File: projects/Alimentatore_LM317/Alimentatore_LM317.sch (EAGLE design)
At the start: 19 parts, among them X1 SMKDSP_1,5/3, X2 SMKDSP_1,5/3

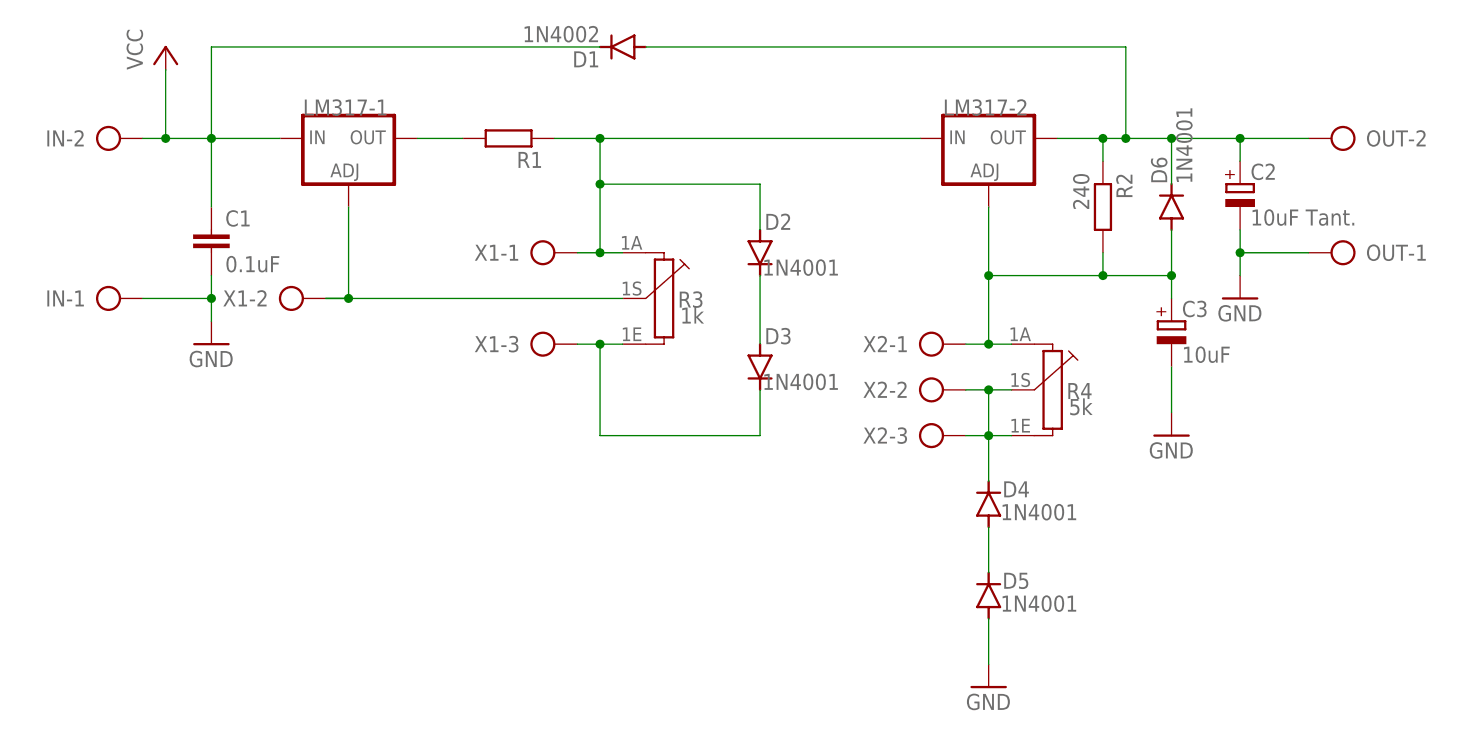
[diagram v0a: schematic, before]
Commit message: aggiunti circuiti alternativi LM317.
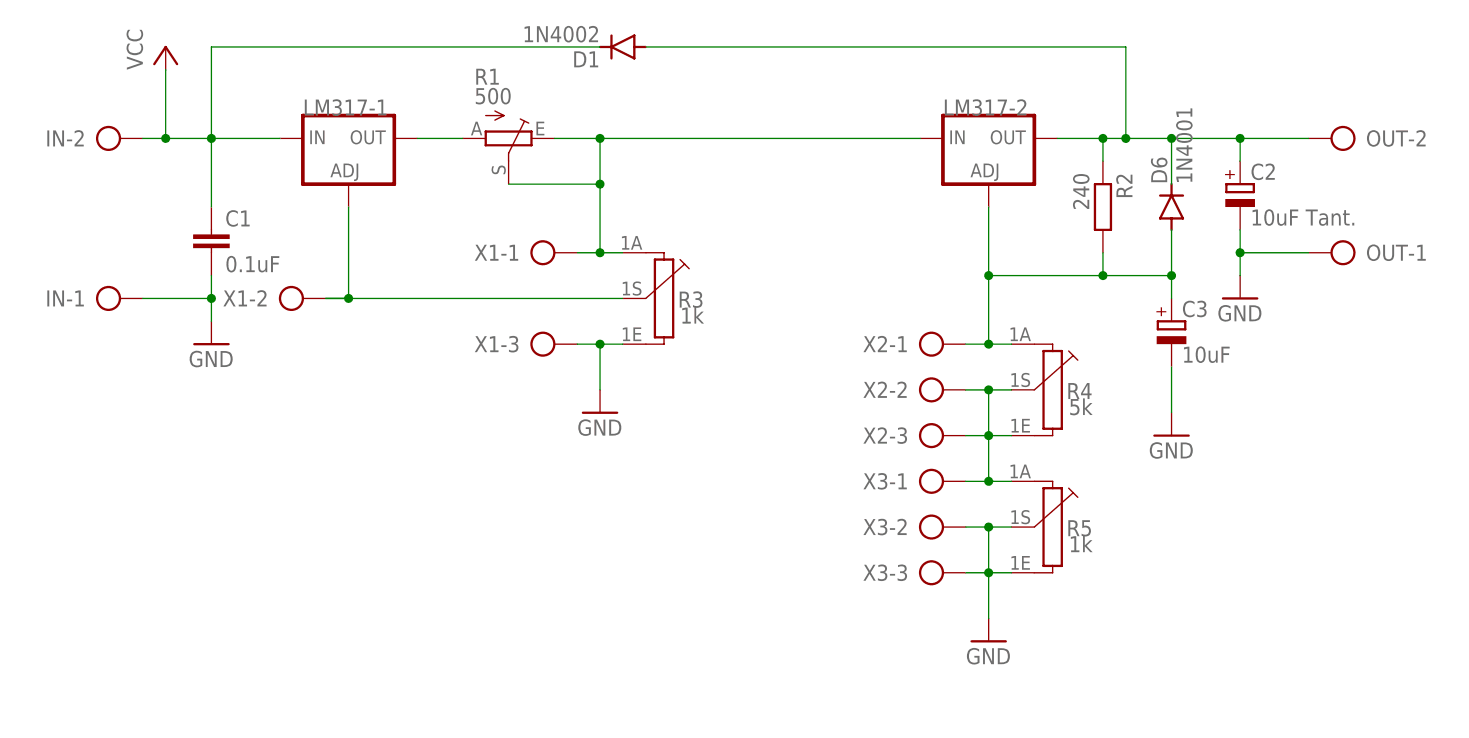
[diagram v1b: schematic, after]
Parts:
- removed D2, D3, D4, D5: 1N4001, diode_MOD:1N4004DO-41
- added R5: 1k, piher:PC16S
- added X3: SMKDSP_1,5/3, con-phoenix-smkdsp:SMKDSP_1,5/3
- R1: value (none) -> 500; device rcl:R-EU_0204/7 -> pot:TRIM_EU-CA6V
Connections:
- removed net N$10: D4.C, R4.1E, R4.1S, X2-2.KL, X2-3.KL
- removed net N$6: D4.A, D5.C
- removed net N$7: D3.C, R3.1E, X1-3.KL
- net GND: now also R3.1E, R5.1E, R5.1S, X1-3.KL, X3-2.KL, X3-3.KL; no longer D5.A
- net N$2: now also R1.A; no longer R1.2
- net N$3: now also R1.E, R1.S; no longer D2.A, R1.1
- net N$4: now also R4.1E, R4.1S, R5.1A, X2-2.KL, X2-3.KL, X3-1.KL; no longer D2.C, D3.A
